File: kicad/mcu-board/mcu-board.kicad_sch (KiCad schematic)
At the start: 40 parts, among them J1 Conn_01x03, J10 Conn_01x03, J11 Conn_01x02, J12 Conn_01x02, J13 UJ20-C-H-G-SMT-P16-TR, J3 Conn_01x03, J4 Conn_01x10, J6 Conn_01x03, J7 Conn_01x03, J8 Conn_01x04, J9 Conn_01x02, SW1 SW_Push, U2 Lora1276-C1-868, U3 ESP32-S3-WROOM-1U-N16R8

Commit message: chore?: Saving just in case I screw up something when redoing the board with battery cutout.
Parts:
- removed J10, J3, J6: Conn_01x03, Connector_PinHeader_2.54mm:PinHeader_1x03_P2.54mm_Vertical, symbol Connector_Generic:Conn_01x03
- removed J4: Conn_01x10, Connector_PinHeader_2.54mm:PinHeader_1x10_P2.54mm_Vertical, symbol Connector_Generic:Conn_01x10
- added J10: Conn_01x01, Connector_PinHeader_2.54mm:PinHeader_1x01_P2.54mm_Vertical, symbol Connector_Generic:Conn_01x01
- added J3, J5, J6: Conn_01x02, Connector_PinHeader_2.54mm:PinHeader_1x02_P2.54mm_Vertical, symbol Connector_Generic:Conn_01x02
- added J4: Conn_01x06, Connector_PinHeader_2.54mm:PinHeader_1x06_P2.54mm_Vertical, symbol Connector_Generic:Conn_01x06
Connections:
- net ADC1_CH2: now also J4.2 (Pin_2)
- net GND: now also J10.1 (Pin_1), J4.1 (Pin_1)
- net GPIO39: now also J4.3 (Pin_3)
- net GPIO40: now also J4.4 (Pin_4)
- net GPIO41: now also J4.5 (Pin_5)
- net GPIO42: now also J4.6 (Pin_6)
- net I2CEXT0_SCL: now also J5.2 (Pin_2)
- net I2CEXT0_SDA: now also J5.1 (Pin_1)
- net I2CEXT1_SCL: now also J6.2 (Pin_2)
- net I2CEXT1_SDA: now also J6.1 (Pin_1)
- net U1RX: now also J3.1 (Pin_1)
- net U1TX: now also J3.2 (Pin_2)
- net ANT: now reaches U2.9 (ANT)
- net GPIO45: no longer names the net of U3.26 (IO45)
- net GPIO46: no longer names the net of U3.16 (IO46)
- net GPIO47: no longer names the net of U3.24 (IO47)
- net GPIO48: no longer names the net of U3.25 (IO48)
- no-connect marks 6 -> 10
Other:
- note added: "GND is needed here because we might be passing to an external debug board."
- note added: "The boards will all have the same ground so gnd is passed only once"

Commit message: chore?: Saving again, might redo pcb
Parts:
- removed J1: Conn_01x03, Connector_PinHeader_2.54mm:PinHeader_1x03_P2.54mm_Vertical, symbol Connector_Generic:Conn_01x03
- removed TP9: TestPoint, TestPoint:TestPoint_Pad_D1.0mm, symbol Connector:TestPoint
- added C7: 0.1uf, Capacitor_SMD:C_0805_2012Metric, symbol Device:C
- added R11: 5.1k, Resistor_SMD:R_0805_2012Metric, symbol Device:R
- added TP1, TP15, TP16: TestPoint, TestPoint:TestPoint_Pad_D1.0mm, symbol Connector:TestPoint
- H1, H2, H3: footprint MountingHole:MountingHole_3mm_Pad -> PSAT_Library:Mounting-Hole-3mm-0.05mm-pad
- renumbered C2 to C1, C1 to C2, J11 to J10, J12 to J11, J13 to J12, J4 to J2, J10 to J3, J3 to J4, R3 to R1, R5 to R2, R4 to R3, R6 to R4, R9 to R5, R10 to R6, TP11 to TP10, TP10 to TP11, TP8 to TP2, TP7 to TP3, TP2 to TP4, TP3 to TP5, TP4 to TP6, TP5 to TP7, TP1 to TP8, TP6 to TP9, U2 to U1, U3 to U2
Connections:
- net +3V3: now also R1.2, R2.2, R3.1, R4.1, R11.2; no longer SW1.1
- net ESP_RESET: now also C7.1, R11.1
- net GND: now also SW1.1, C7.2, TP1.1
- net I2CEXT0_SCL: now also TP3.1; no longer R4.2
- net I2CEXT0_SDA: now also TP2.1; no longer R2.1
- net I2CEXT1_SCL: now also R4.2, TP16.1
- net I2CEXT1_SDA: now also R2.1, TP15.1
- net ADC1_CH0: no longer names the net of U2.27 (IO0)
- net U0RX: no longer names the net of U2.36 (RXD0)
- net U0TX: no longer names the net of U2.37 (TXD0)
- no-connect marks 10 -> 13
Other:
- note added: "Allegedly no pullups required to set the speed. Defaults to usb 2.0 - full-speed"
- note added: "D- and D+ Support usbserial out over uart0. GPIO Pins 22-37 are probably internally used for ram/flash"
- note removed: "ADC For Battery Voltage Reading"
- note removed: "D- and D+ Support usbserial out over uart0. Uart0 otherwise is not exposed GPIO Pins 22-37 are probably internally used for ram/flash"
- note removed: "GND is needed here because we might be passing to an external debug board."
- note removed: "Optional Debug Output"
- moved on the sheet: J12, R5, R6, SW1, TP11, TP2, TP3

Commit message: feat: finished the mcu-board?
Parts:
- added SW2: SW_Push, Button_Switch_SMD:SW_Push_1P1T_NO_CK_KMR2, symbol Switch:SW_Push
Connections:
- net GND: now also SW2.1
- net DI4: now reaches TP7.1, U1.12 (DI4)
- net DI2: now reaches TP5.1, U1.16 (DI2)
- net at U2.27 (IO0): now also SW2.2
- net DI3: now reaches TP6.1, U1.11 (DI3)
- net DI1: now reaches TP4.1, U1.15 (DI1)
- net DI5: now reaches TP9.1, U1.7 (DI5)
- no-connect marks 13 -> 12
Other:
- note added: "Flash Button"
- moved on the sheet: TP10
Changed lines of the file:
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@@
 		)
 	)
+	(text "Flash Button"
+		(exclude_from_sim no)
+		(at 112.268 81.534 0)
+		(effects
+			(font
+				(size 1.27 1.27)
+			)
+		)
+	)
 	(text "D- and D+ Support usbserial out over uart0.\nGPIO Pins 22-37 are probably internally used for ram/flash\n"
 		(exclude_from_sim no)
@@
 	)
 	(no_connect
-		(at 128.27 85.09)
-	)
-	(no_connect
 		(at 236.22 53.34)
 	)
@@
 	(wire
 		(pts
+			(xy 127 85.09) (xy 128.27 85.09)
+		)
+		(stroke
+			(width 0)
+			(type default)
+		)
+	)
+	(wire
+		(pts
 			(xy 242.57 35.56) (xy 236.22 35.56)
 		)
@@
 		)
 	)
+	(label "DI3"
+		(at 74.93 165.1 0)
+		(effects
+			(font
+				(size 1.27 1.27)
+			)
+			(justify left bottom)
+		)
+	)
 	(label "I2CEXT1_SCL"
 		(at 115.57 118.11 0)
@@
 		)
 	)
+	(label "DI5"
+		(at 74.93 170.18 0)
+		(effects
+			(font
+				(size 1.27 1.27)
+			)
+			(justify left bottom)
+		)
+	)
 	(label "U1TX"
 		(at 66.04 71.12 0)
@@
 		)
 	)
+	(label "DI2"
+		(at 74.93 162.56 0)
+		(effects
+			(font
+				(size 1.27 1.27)
+			)
+			(justify left bottom)
+		)
+	)
 	(label "POWER_ST"
 		(at 170.18 80.01 180)
@@
 		)
 	)
+	(label "DI4"
+		(at 74.93 167.64 0)
+		(effects
+			(font
+				(size 1.27 1.27)
+			)
+			(justify left bottom)
+		)
+	)
 	(label "SERVO_PWM"
 		(at 115.57 105.41 0)
@@
 		)
 	)
+	(label "DI1"
+		(at 74.93 160.02 0)
+		(effects
+			(font
+				(size 1.27 1.27)
+			)
+			(justify left bottom)
+		)
+	)
 	(label "SERVO_PWM"
 		(at 67.31 83.82 0)
@@
 	)
 	(symbol
+		(lib_id "power:GND")
+		(at 116.84 85.09 270)
+		(unit 1)
+		(exclude_from_sim no)
+		(in_bom yes)
+		(on_board yes)
+		(dnp no)
+		(fields_autoplaced yes)
+		(property "Reference" "#PWR02"
+			(at 110.49 85.09 0)
+			(effects
+				(font
+					(size 1.27 1.27)
+				)
+				(hide yes)
+			)
+		)
+		(property "Value" "GND"
+			(at 113.03 85.0899 90)
+			(effects
+				(font
+					(size 1.27 1.27)
+				)
+				(justify right)
+			)
+		)
+		(property "Footprint" ""
+			(at 116.84 85.09 0)
+			(effects
+				(font
+					(size 1.27 1.27)
+				)
+				(hide yes)
+			)
+		)
+		(property "Datasheet" ""
+			(at 116.84 85.09 0)
+			(effects
+				(font
+					(size 1.27 1.27)
+				)
+				(hide yes)
+			)
+		)
+		(property "Description" "Power symbol creates a global label with name \"GND\" , ground"
+			(at 116.84 85.09 0)
+			(effects
+				(font
+					(size 1.27 1.27)
+				)
+				(hide yes)
+			)
+		)
+		(pin "1"
+		)
+		(instances
+			(project "mcu-board"
+				(path "/f6735569-a094-4d1f-804a-28898efbaebf"
+					(reference "#PWR02")
+					(unit 1)
+				)
+			)
+		)
+	)
+	(symbol
 		(lib_id "Connector:TestPoint")
 		(at 113.03 87.63 0)
-		(mirror y)
+		(mirror x)
 		(unit 1)
 		(exclude_from_sim no)
@@
 		(dnp no)
 		(property "Reference" "TP10"
-			(at 110.49 84.3279 0)
+			(at 106.68 91.186 0)
 			(effects
 				(font
@@
 		)
 		(property "Value" "TestPoint"
-			(at 110.49 85.5979 0)
+			(at 115.57 89.6621 0)
 			(effects
 				(font
@@
 		)
 		(property "Footprint" "TestPoint:TestPoint_Pad_D1.0mm"
-			(at 107.95 87.63 0)
+			(at 118.11 87.63 0)
 			(effects
 				(font
@@
 		)
 		(property "Datasheet" "~"
-			(at 107.95 87.63 0)
+			(at 118.11 87.63 0)
 			(effects
 				(font
@@
 					(unit 1)
 				)
+			)
+		)
+	)
+	(symbol
+		(lib_id "Switch:SW_Push")
+		(at 121.92 85.09 0)
+		(unit 1)
+		(exclude_from_sim no)
+		(in_bom yes)
+		(on_board yes)
+		(dnp no)
+		(property "Reference" "SW2"
+			(at 121.92 80.01 0)
+			(effects
+				(font
+					(size 1.27 1.27)
+				)
+			)
+		)
+		(property "Value" "SW_Push"
+			(at 121.92 80.01 0)
+			(effects
+				(font
+					(size 1.27 1.27)
+				)
+				(hide yes)
+			)
+		)
+		(property "Footprint" "Button_Switch_SMD:SW_Push_1P1T_NO_CK_KMR2"
+			(at 121.92 80.01 0)
+			(effects
+				(font
+					(size 1.27 1.27)
+				)
+				(hide yes)
+			)
+		)
+		(property "Datasheet" "~"
+			(at 121.92 80.01 0)
+			(effects
+				(font
+					(size 1.27 1.27)
+				)
+				(hide yes)
+			)
+		)
+		(property "Description" "Push button switch, generic, two pins"
+			(at 121.92 85.09 0)
+			(effects
+				(font
+					(size 1.27 1.27)
+				)
+				(hide yes)
+			)
+		)
+		(pin "2"
+		)
+		(pin "1"
+		)
+		(instances
+			(project "mcu-board"
+				(path "/f6735569-a094-4d1f-804a-28898efbaebf"
+					(reference "SW2")
+					(unit 1)
+				)

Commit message: chore: Fixed led footprint from 0805 to 0603, and edited title for buzzer
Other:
- company: The Retrievers -> The Retrievers | Designed by aids
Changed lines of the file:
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@@
 		(date "2025-12-10")
 		(rev "V1")
-		(company "The Retrievers")
+		(company "The Retrievers | Designed by aids")
 	)
 	(rectangle

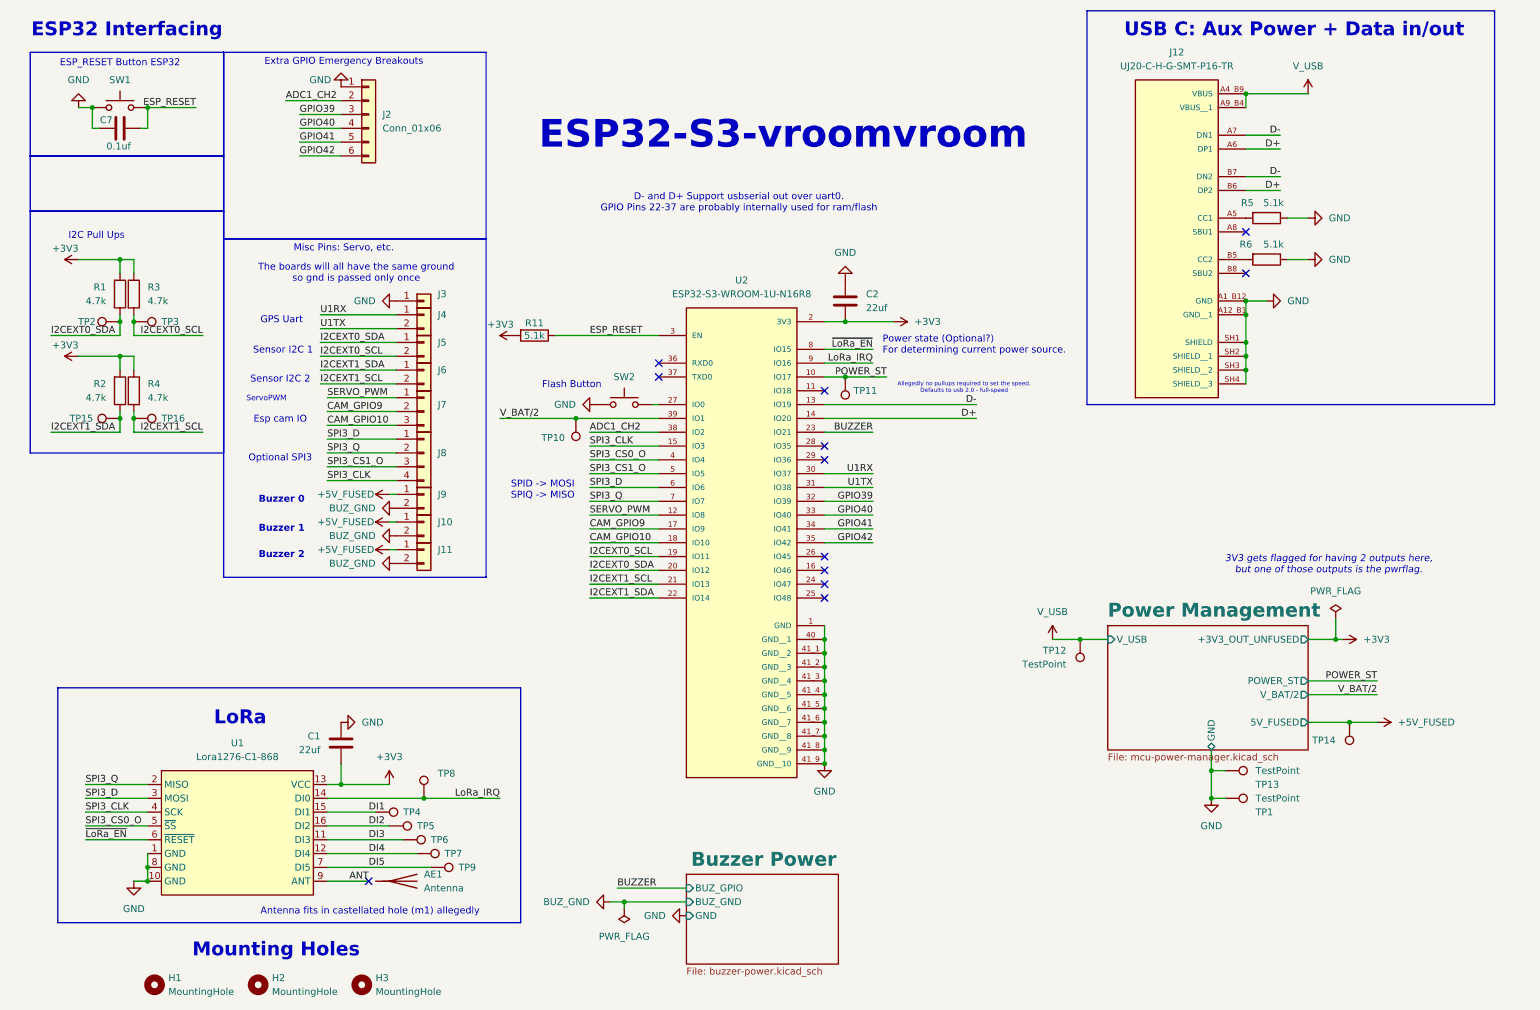
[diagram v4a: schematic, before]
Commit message: feat: finished v2 schematic of mcu-board
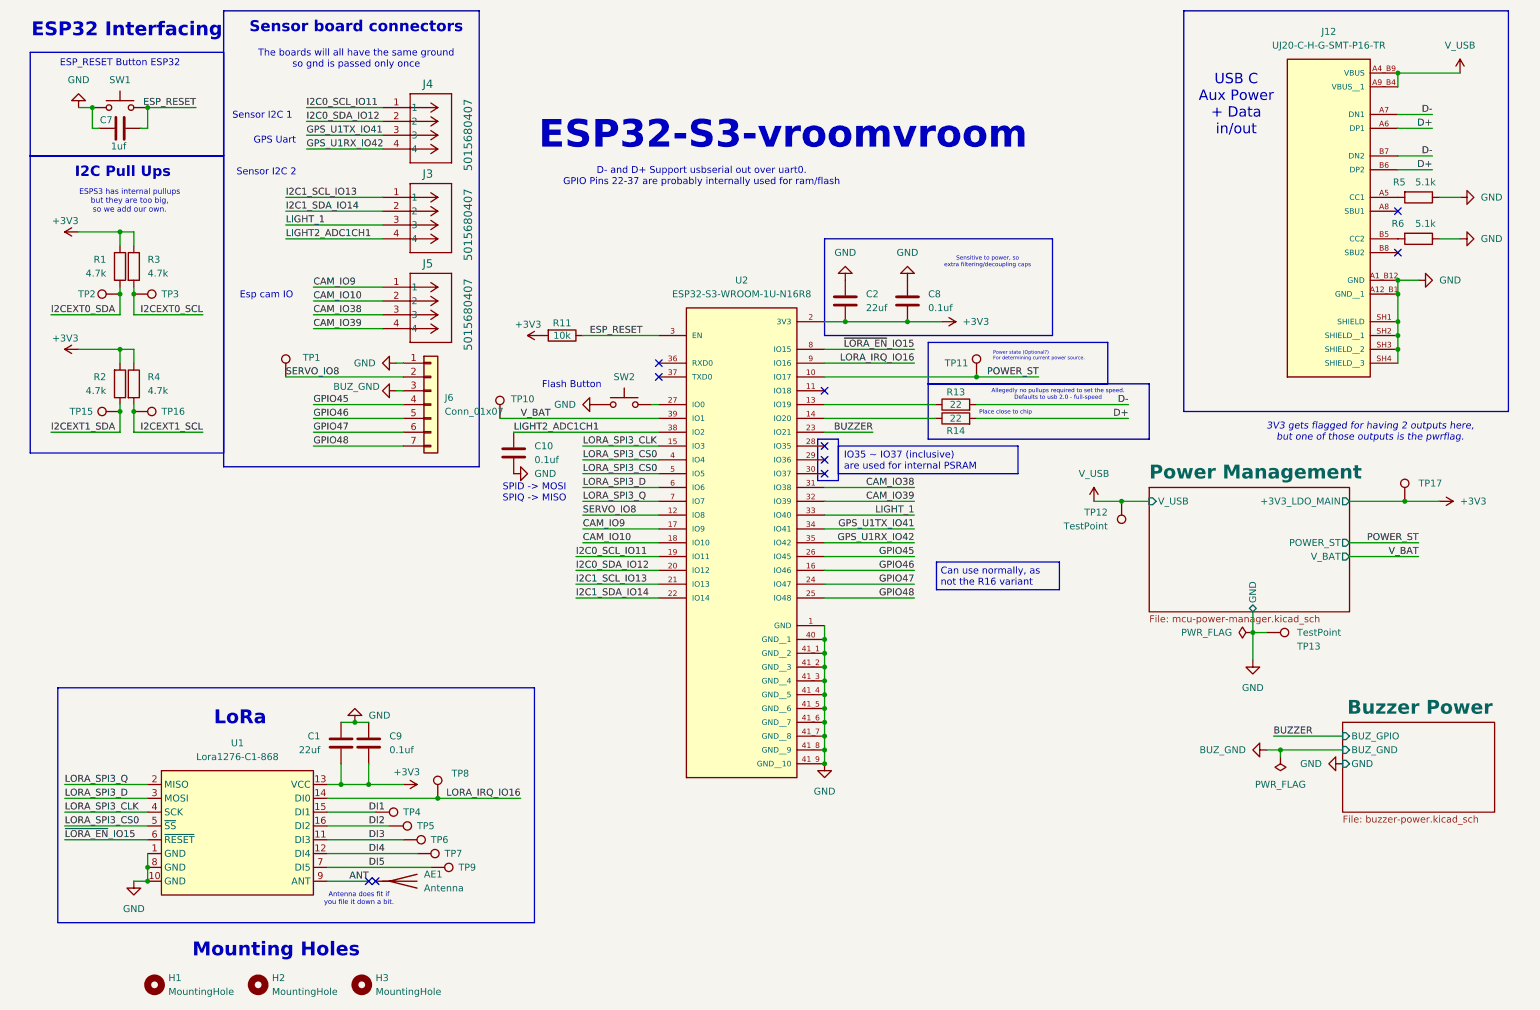
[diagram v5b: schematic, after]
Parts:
- removed J10, J11, J4, J5, J6, J9: Conn_01x02, Connector_PinHeader_2.54mm:PinHeader_1x02_P2.54mm_Vertical, symbol Connector_Generic:Conn_01x02
- removed J2: Conn_01x06, Connector_PinHeader_2.54mm:PinHeader_1x06_P2.54mm_Vertical, symbol Connector_Generic:Conn_01x06
- removed J3: Conn_01x01, Connector_PinHeader_2.54mm:PinHeader_1x01_P2.54mm_Vertical, symbol Connector_Generic:Conn_01x01
- removed J7: Conn_01x03, Connector_PinHeader_2.54mm:PinHeader_1x03_P2.54mm_Vertical, symbol Connector_Generic:Conn_01x03
- removed J8: Conn_01x04, Connector_PinHeader_2.54mm:PinHeader_1x04_P2.54mm_Vertical, symbol Connector_Generic:Conn_01x04
- removed TP14: TestPoint, TestPoint:TestPoint_Pad_D1.0mm, symbol Connector:TestPoint
- added C10, C8, C9: 0.1uf, Capacitor_SMD:C_0805_2012Metric, symbol Device:C
- added J3, J4, J5: 5015680407, CONN_5015680000-SD_04_MOL, symbol 2026-01-26_05-30-52:5015680407
- added J6: Conn_01x07, symbol Connector_Generic:Conn_01x07
- added R13, R14: 22, symbol Device:R
- added TP17: TestPoint, TestPoint:TestPoint_Pad_D1.0mm, symbol Connector:TestPoint
- C7: value 0.1uf -> 1uf
- R11: value 5.1k -> 10k
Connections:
- net SPI3_CS1_O is gone; now on net LORA_SPI3_CS0: U2.5 (IO5)
- net +3V3: now also C8.1, C9.1, TP17.1
- net BUZ_GND: now also J6.3 (Pin_3)
- net D+: now also R14.2; no longer U2.14 (IO20)
- net D-: now also R13.2; no longer U2.13 (IO19)
- net GND: now also C10.1, C8.2, C9.2, J6.1 (Pin_1); no longer TP1.1
- net I2CEXT0_SCL: no longer U2.19 (IO11)
- net I2CEXT0_SDA: no longer U2.20 (IO12)
- net I2CEXT1_SCL: no longer U2.21 (IO13)
- net I2CEXT1_SDA: no longer U2.22 (IO14)
- net GPIO46: now reaches U2.16 (IO46)
- net GPIO46: now also J6.5 (Pin_5)
- net GPIO47: now reaches U2.24 (IO47)
- net GPIO47: now also J6.6 (Pin_6)
- net GPIO48: now reaches U2.25 (IO48)
- net GPIO48: now also J6.7 (Pin_7)
- net GPIO45: now reaches U2.26 (IO45)
- net GPIO45: now also J6.4 (Pin_4)
- net ADC1_CH2 renamed LIGHT2_ADC1CH1
- net LIGHT2_ADC1CH1: now also C10.2, J3.4
- net CAM_GPIO10 renamed CAM_IO10
- net CAM_IO10: now also J5.2
- net CAM_GPIO9 renamed CAM_IO9
- net CAM_IO9: now also J5.1
- net GPIO39 renamed CAM_IO39
- net CAM_IO39: now also J5.4
- net GPIO40 renamed LIGHT_1
- net LIGHT_1: now also J3.3
- net GPIO41 renamed GPS_U1TX_IO41
- net GPS_U1TX_IO41: now also J4.3
- net GPIO42 renamed GPS_U1RX_IO42
- net GPS_U1RX_IO42: now also J4.4
- net LoRa_IRQ renamed LORA_IRQ_IO16
- net SERVO_PWM renamed SERVO_IO8
- net SERVO_IO8: now also TP1.1, J6.2 (Pin_2)
- net SPI3_CLK renamed LORA_SPI3_CLK
- net SPI3_CS0_O renamed LORA_SPI3_CS0
- net SPI3_D renamed LORA_SPI3_D
- net SPI3_Q renamed LORA_SPI3_Q
- net U1RX: no longer names the net of U2.30 (IO37)
- net U1TX renamed CAM_IO38
- net CAM_IO38: now also J5.3
- net V_BAT/2 renamed V_BAT
- net ~{LoRa_EN} renamed ~{LORA_EN}_IO15
- new net: R13.1, U2.13 (IO19)
- new net: R14.1, U2.14 (IO20)
- new net I2C0_SCL_IO11: J4.1, U2.19 (IO11)
- new net I2C0_SDA_IO12: J4.2, U2.20 (IO12)
- new net I2C1_SCL_IO13: J3.1, U2.21 (IO13)
- new net I2C1_SDA_IO14: J3.2, U2.22 (IO14)
- no-connect marks 12 -> 10
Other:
- sheet Power Management ports: added +3V3_LDO_MAIN, V_BAT; removed +3V3_OUT_UNFUSED, 5V_FUSED, V_BAT/2
- note added: "Antenna does fit if you file it down a bit."
- note added: "Can use normally, as not the R16 variant"
- note added: "ESPS3 has internal pullups but they are too big, so we add our own."
- note added: "IO35 ~ IO37 (inclusive) are used for internal PSRAM"
- note added: "Place close to chip"
- note added: "Sensitive to power, so extra filtering/decoupling caps"
- note added: "Sensor board connectors"
- note added: "USB C Aux Power + Data in/out"
- note removed: "Antenna fits in castellated hole (m1) allegedly"
- note removed: "Buzzer 0"
- note removed: "Buzzer 1"
- note removed: "Buzzer 2"
- note removed: "Extra GPIO Emergency Breakouts"
- note removed: "Misc Pins: Servo, etc."
- note removed: "Optional SPI3"
- note removed: "ServoPWM"
- note removed: "USB C: Aux Power + Data in/out"
- moved on the sheet: J12, R1, R11, R2, R3, R4, R5, R6, TP10, TP11, TP12, TP13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
